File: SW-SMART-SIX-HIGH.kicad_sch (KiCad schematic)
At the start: 98 parts, among them J1 SWD, J2 USART2, J3 POWER OUT, J4 POWER IN, J5 POWER OUT, SW0 BTS7002-1EPP, SW1 BTS7002-1EPP, SW2 BTS7002-1EPP, SW3 BTS7002-1EPP, SW4 BTS7002-1EPP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

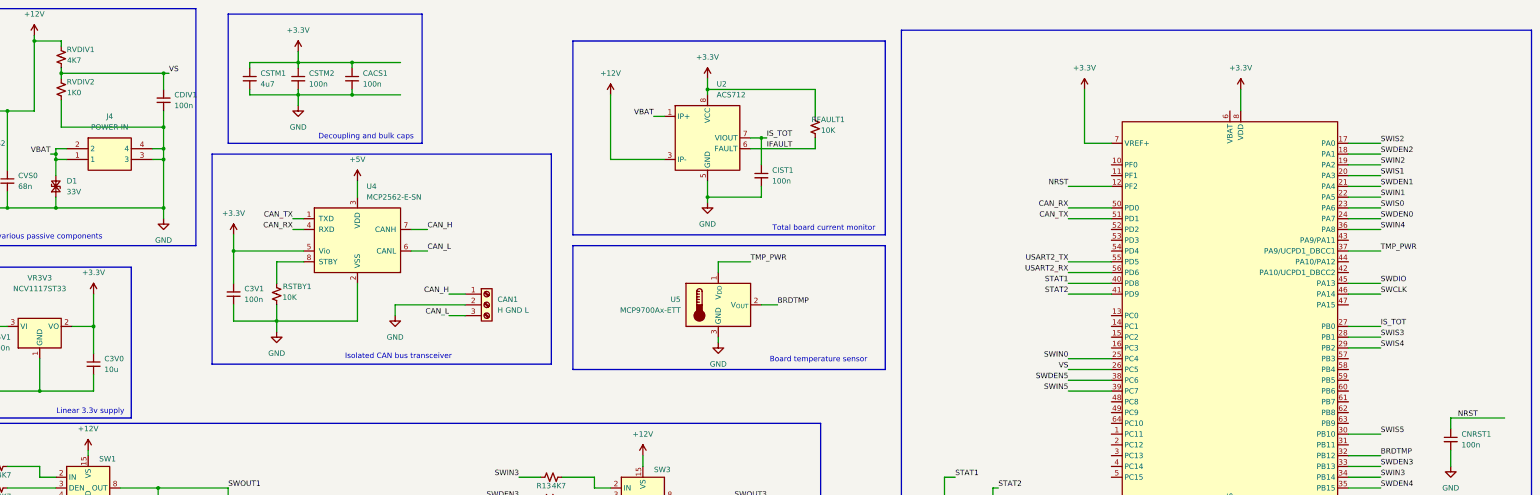
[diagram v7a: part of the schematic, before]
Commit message: added board temp sensor
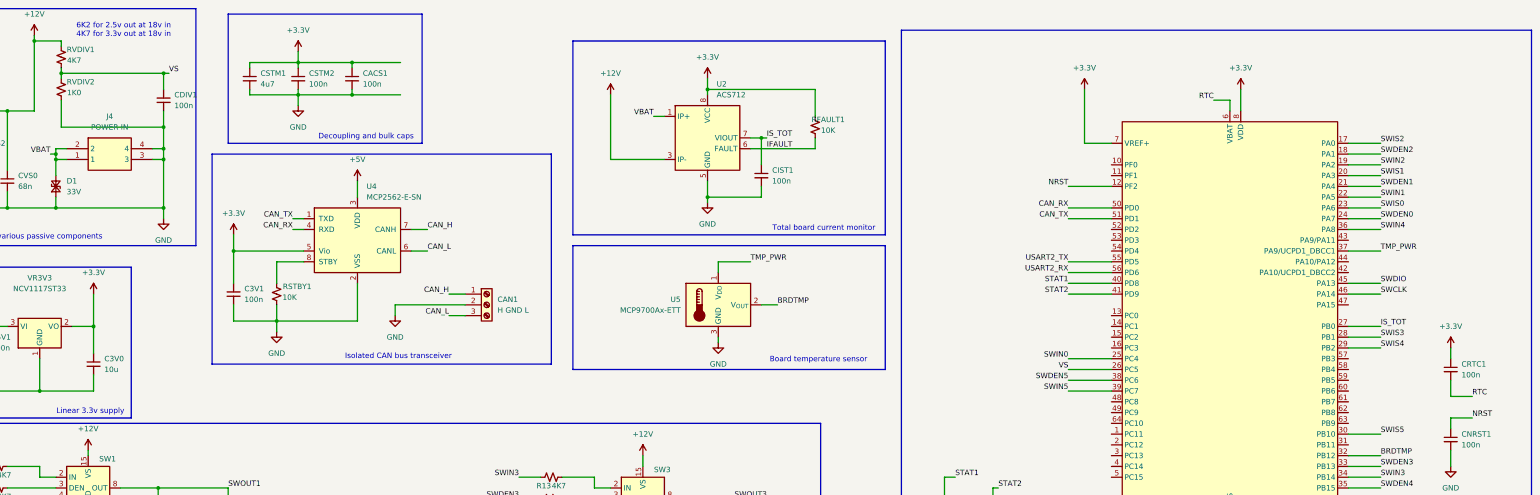
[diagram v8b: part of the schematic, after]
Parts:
- added CRTC1: 100n, Capacitor_SMD:C_0603_1608Metric_Pad1.08x0.95mm_HandSolder, symbol Device:C_Small
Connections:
- net +3.3V: now also CRTC1.1
- net RTC: now reaches U1.6 (VBAT)
- net RTC: now also CRTC1.2
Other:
- note added: "6K2 for 2.5v out at 18v in 4K7 for 3.3v out at 18v in"
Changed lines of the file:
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@@
 		)
 	)
+	(text "6K2 for 2.5v out at 18v in\n4K7 for 3.3v out at 18v in"
+		(exclude_from_sim no)
+		(at 72.136 19.05 0)
+		(effects
+			(font
+				(size 1.27 1.27)
+			)
+			(justify left)
+		)
+	)
 	(text "Total board current monitor"
 		(exclude_from_sim no)
@@
 	(wire
 		(pts
-			(xy 396.24 110.49) (xy 408.94 110.49)
+			(xy 396.24 110.49) (xy 401.32 110.49)
 		)
 		(stroke
@@
 	(wire
 		(pts
+			(xy 396.24 105.41) (xy 401.32 105.41)
+		)
+		(stroke
+			(width 0)
+			(type default)
+		)
+	)
+	(wire
+		(pts
 			(xy 107.95 224.79) (xy 107.95 228.6)
 		)
@@
 	(wire
 		(pts
+			(xy 396.24 93.98) (xy 396.24 96.52)
+		)
+		(stroke
+			(width 0)
+			(type default)
+		)
+	)
+	(wire
+		(pts
 			(xy 392.43 213.36) (xy 392.43 205.74)
 		)
@@
 	(wire
 		(pts
+			(xy 396.24 101.6) (xy 396.24 105.41)
+		)
+		(stroke
+			(width 0)
+			(type default)
+		)
+	)
+	(wire
+		(pts
 			(xy 220.98 58.42) (xy 220.98 59.69)
 		)
@@
 	(wire
 		(pts
+			(xy 340.36 35.56) (xy 344.17 35.56)
+		)
+		(stroke
+			(width 0)
+			(type default)
+		)
+	)
+	(wire
+		(pts
 			(xy 340.36 217.17) (xy 340.36 219.71)
 		)
@@
 	(wire
 		(pts
+			(xy 344.17 35.56) (xy 344.17 38.1)
+		)
+		(stroke
+			(width 0)
+			(type default)
+		)
+	)
+	(wire
+		(pts
 			(xy 372.11 88.9) (xy 379.73 88.9)
 		)
@@
 	)
 	(label "NRST"
-		(at 402.59 110.49 180)
+		(at 401.32 110.49 0)
 		(effects
 			(font
 				(size 1.27 1.27)
 			)
-			(justify right bottom)
+			(justify left bottom)
 		)
 	)
@@
 		)
 	)
+	(label "RTC"
+		(at 340.36 35.56 180)
+		(effects
+			(font
+				(size 1.27 1.27)
+			)
+			(justify right bottom)
+		)
+	)
 	(label "SW"
 		(at 354.33 199.39 0)
@@
 		)
 	)
+	(label "RTC"
+		(at 401.32 105.41 0)
+		(effects
+			(font
+				(size 1.27 1.27)
+			)
+			(justify left bottom)
+		)
+	)
 	(label "SWDEN1"
 		(at 379.73 55.88 0)
@@
 	)
 	(symbol
+		(lib_id "Device:C_Small")
+		(at 396.24 99.06 0)
+		(unit 1)
+		(exclude_from_sim no)
+		(in_bom yes)
+		(on_board yes)
+		(dnp no)
+		(fields_autoplaced yes)
+		(property "Reference" "CRTC1"
+			(at 398.78 97.7962 0)
+			(effects
+				(font
+					(size 1.27 1.27)
+				)
+				(justify left)
+			)
+		)
+		(property "Value" "100n"
+			(at 398.78 100.3362 0)
+			(effects
+				(font
+					(size 1.27 1.27)
+				)
+				(justify left)
+			)
+		)
+		(property "Footprint" "Capacitor_SMD:C_0603_1608Metric_Pad1.08x0.95mm_HandSolder"
+			(at 396.24 99.06 0)
+			(effects
+				(font
+					(size 1.27 1.27)
+				)
+				(hide yes)
+			)
+		)
+		(property "Datasheet" "~"
+			(at 396.24 99.06 0)
+			(effects
+				(font
+					(size 1.27 1.27)
+				)
+				(hide yes)
+			)
+		)
+		(property "Description" "Unpolarized capacitor, small symbol"
+			(at 396.24 99.06 0)
+			(effects
+				(font
+					(size 1.27 1.27)
+				)
+				(hide yes)
+			)
+		)
+		(pin "2"
+		)
+		(pin "1"
+		)
+		(instances
+			(project "SW-SMART-SIX-HIGH"
+				(path "/08d9f551-d314-4c5c-859f-da02a807087d"
+					(reference "CRTC1")
+					(unit 1)
+				)
+			)
+		)
+	)
+	(symbol
 		(lib_id "Device:R_Small_US")
 		(at 194.31 194.31 180)
@@
 					(unit 1)
 				)
+			)
+		)
+	)
+	(symbol
+		(lib_id "power:+3.3V")
+		(at 396.24 93.98 0)
+		(unit 1)
+		(exclude_from_sim no)
+		(in_bom yes)
+		(on_board yes)
+		(dnp no)
+		(property "Reference" "#PWR045"
+			(at 396.24 97.79 0)
+			(effects
+				(font
+					(size 1.27 1.27)
+				)
+				(hide yes)
+			)
+		)
+		(property "Value" "+3.3V"
+			(at 396.24 88.9 0)
+			(effects
+				(font
+					(size 1.27 1.27)
+				)
+			)
+		)
+		(property "Footprint" ""
+			(at 396.24 93.98 0)
+			(effects
+				(font
+					(size 1.27 1.27)
+				)
+				(hide yes)
+			)
+		)
+		(property "Datasheet" ""
+			(at 396.24 93.98 0)
+			(effects
+				(font
+					(size 1.27 1.27)
+				)
+				(hide yes)
+			)
+		)
+		(property "Description" "Power symbol creates a global label with name \"+3.3V\""
+			(at 396.24 93.98 0)
+			(effects
+				(font
+					(size 1.27 1.27)
+				)
+				(hide yes)
+			)
+		)
+		(pin "1"
+		)
+		(instances
+			(project "SW-SMART-SIX-HIGH"
+				(path "/08d9f551-d314-4c5c-859f-da02a807087d"
+					(reference "#PWR045")
+					(unit 1)
+				)
